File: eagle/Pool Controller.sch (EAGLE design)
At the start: 25 parts, among them J1 POWER_JACKPTH, J2 Temp_Pool, J4 Solar_Mon, J5 Temp_Solar, J6 Temp_Roof

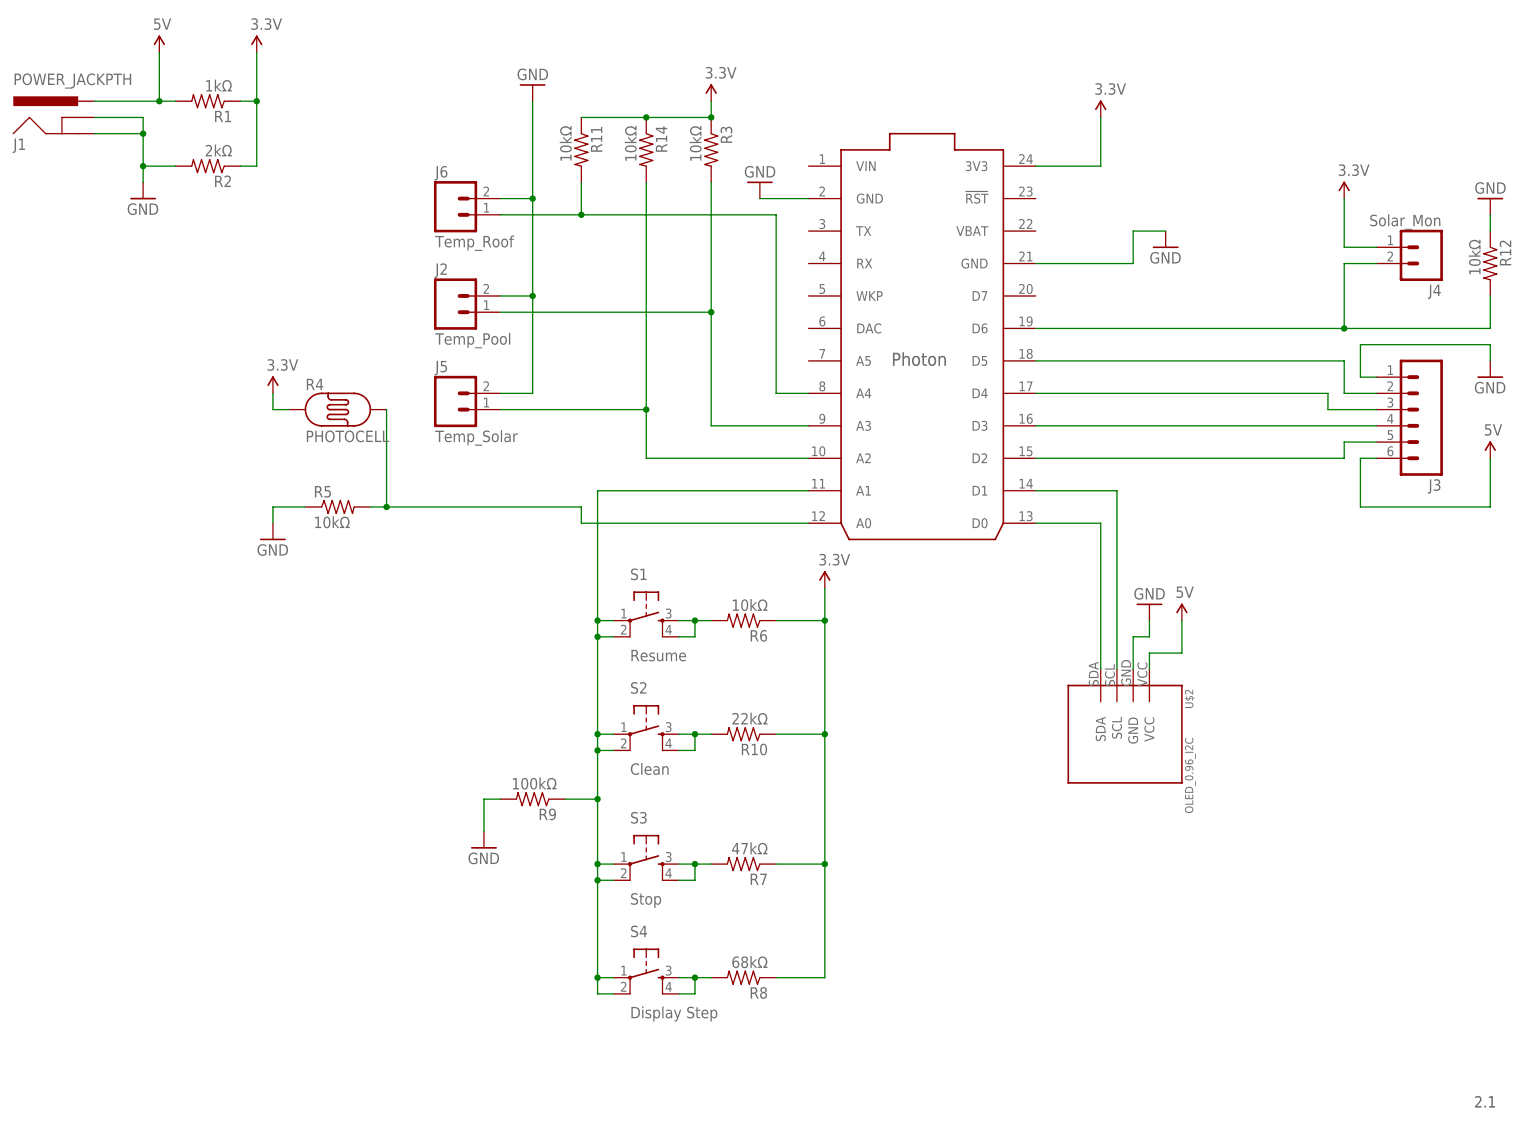
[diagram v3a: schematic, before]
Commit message: corrected relay pinout
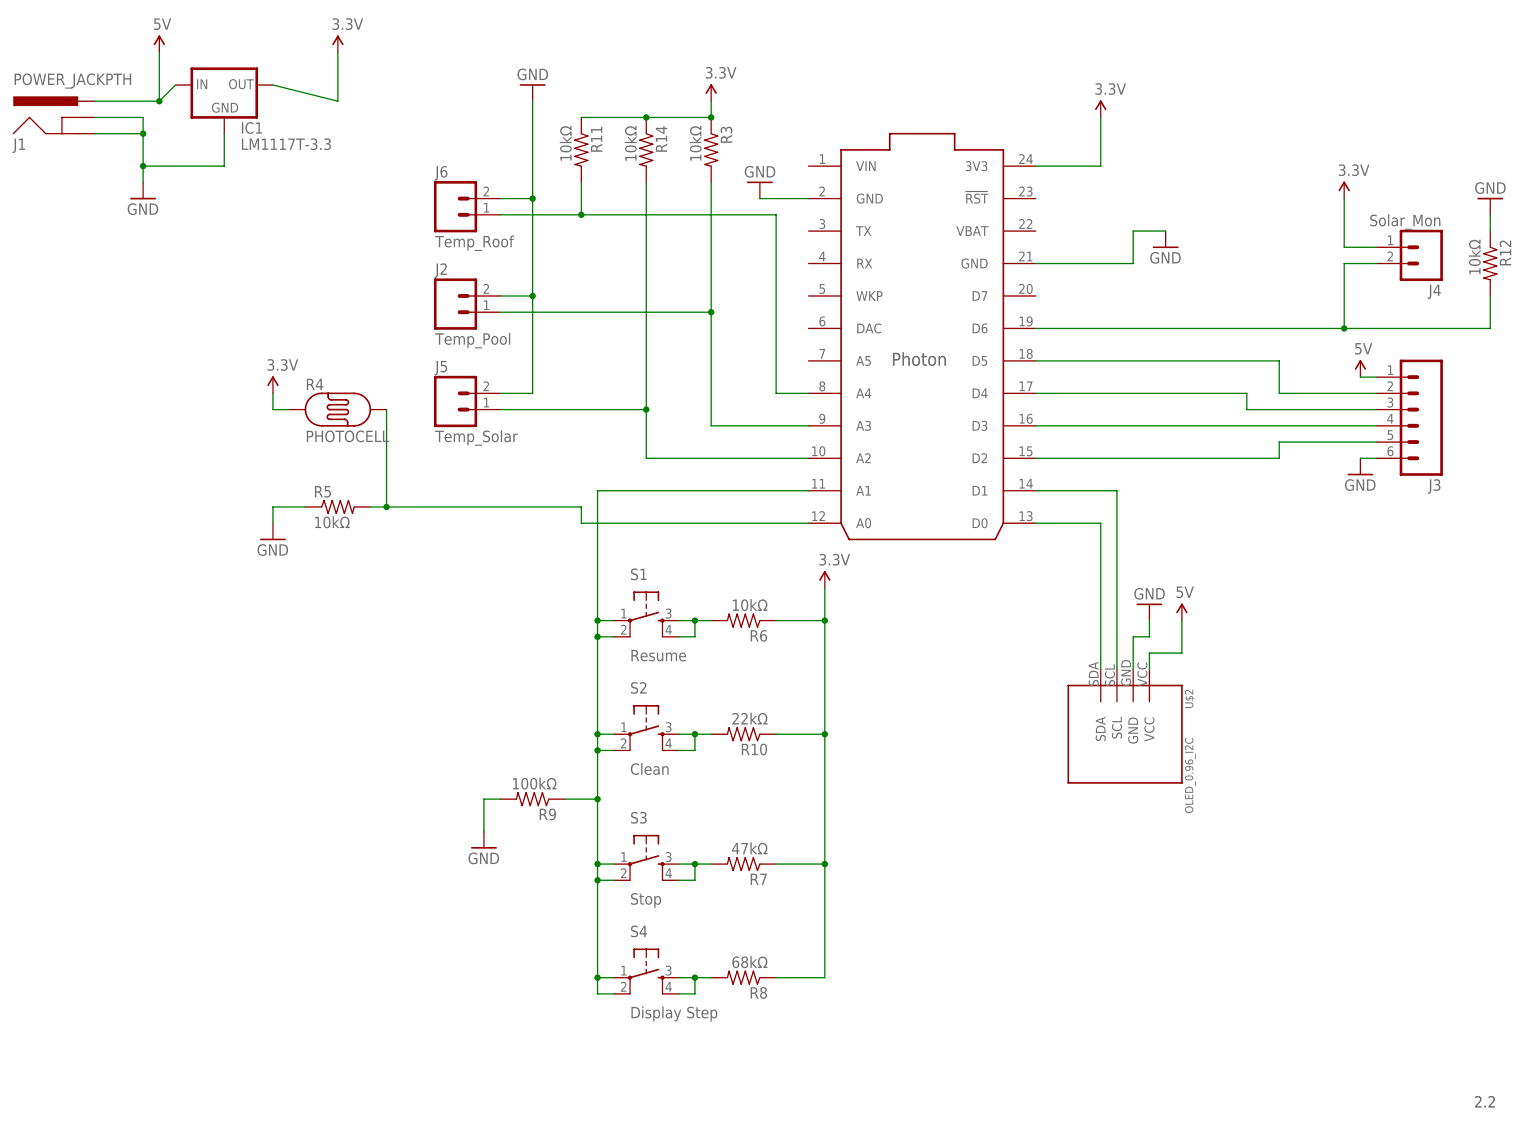
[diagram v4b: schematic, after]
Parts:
- removed R1: 1kΩ, SparkFun-Passives:RESISTORAXIAL-0.3
- removed R2: 2kΩ, SparkFun-Passives:RESISTORAXIAL-0.3
- added IC1: LM1117T-3.3, lm1117:LM1117T-3.3-V
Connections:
- net 3.3V: now also IC1.OUT; no longer R1.1, R2.1
- net 5V: now also IC1.IN, J3.1; no longer J3.6, R1.2
- net GND: now also IC1.GND, J3.6; no longer J3.1, R2.2
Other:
- note added: "2.2"
- note removed: "2.1"
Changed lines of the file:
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@@
 <part name="FRAME1" library="frames" deviceset="LETTER_L" device=""/>
 <part name="J1" library="SparkFun-Connectors" deviceset="POWER_JACK" device="PTH"/>
-<part name="R1" library="SparkFun-Passives" deviceset="RESISTOR" device="AXIAL-0.3" value="1kΩ"/>
-<part name="R2" library="SparkFun-Passives" deviceset="RESISTOR" device="AXIAL-0.3" value="2kΩ"/>
 <part name="R4" library="SparkFun-Sensors" deviceset="PHOTOCELL" device="PTH" value="PHOTOCELL"/>
 <part name="R5" library="SparkFun-Passives" deviceset="RESISTOR" device="AXIAL-0.3" value="10kΩ"/>
@@
 <part name="J6" library="SparkFun-Connectors" deviceset="M02" device="5MM" value="Temp_Roof"/>
 <part name="R11" library="SparkFun-Passives" deviceset="RESISTOR" device="AXIAL-0.3" value="10kΩ"/>
+<part name="IC1" library="lm1117" deviceset="LM1117T-*" device="-V" technology="3.3" value="LM1117T-3.3"/>
 </parts>
 <sheets>
 <sheet>
 <plain>
-<text x="233.68" y="-38.1" size="1.778" layer="97">2.1</text>
+<text x="233.68" y="-38.1" size="1.778" layer="97">2.2</text>
 </plain>
 <instances>
@@
 <instance part="FRAME1" gate="G$2" x="142.24" y="-45.72"/>
 <instance part="J1" gate="G$1" x="15.24" y="111.76"/>
-<instance part="R1" gate="G$1" x="35.56" y="119.38" rot="R180"/>
-<instance part="R2" gate="G$1" x="35.56" y="109.22" rot="R180"/>
 <instance part="R4" gate="G$1" x="55.88" y="71.12"/>
 <instance part="R5" gate="G$1" x="55.88" y="55.88"/>
 <instance part="GND1" gate="1" x="25.4" y="104.14"/>
-<instance part="SUPPLY1" gate="G$1" x="43.18" y="127"/>
+<instance part="SUPPLY1" gate="G$1" x="55.88" y="127"/>
 <instance part="SUPPLY2" gate="G$1" x="175.26" y="116.84"/>
 <instance part="GND2" gate="1" x="121.92" y="106.68" rot="R180"/>
@@
 <instance part="R10" gate="G$1" x="119.38" y="20.32" rot="R180"/>
 <instance part="J3" gate="G$1" x="223.52" y="71.12" rot="R180"/>
-<instance part="GND8" gate="1" x="236.22" y="76.2"/>
-<instance part="SUPPLY8" gate="G$1" x="236.22" y="63.5"/>
+<instance part="GND8" gate="1" x="215.9" y="60.96"/>
+<instance part="SUPPLY8" gate="G$1" x="215.9" y="76.2"/>
 <instance part="J4" gate="G$1" x="226.06" y="96.52" rot="R180"/>
 <instance part="J2" gate="G$1" x="73.66" y="86.36"/>
@@
 <instance part="J6" gate="G$1" x="73.66" y="101.6"/>
 <instance part="R11" gate="G$1" x="93.98" y="111.76" rot="R270"/>
+<instance part="IC1" gate="G$1" x="38.1" y="121.92"/>
 </instances>
 <busses>
@@
 <wire x1="17.78" y1="114.3" x2="25.4" y2="114.3" width="0.1524" layer="91"/>
 <junction x="25.4" y="114.3"/>
-<pinref part="R2" gate="G$1" pin="2"/>
-<wire x1="30.48" y1="109.22" x2="25.4" y2="109.22" width="0.1524" layer="91"/>
 <junction x="25.4" y="109.22"/>
+<pinref part="IC1" gate="G$1" pin="GND"/>
+<wire x1="38.1" y1="114.3" x2="38.1" y2="109.22" width="0.1524" layer="91"/>
+<wire x1="38.1" y1="109.22" x2="25.4" y2="109.22" width="0.1524" layer="91"/>
 </segment>
 <segment>
@@
 <pinref part="GND7" gate="1" pin="GND"/>
 <wire x1="78.74" y1="10.16" x2="78.74" y2="5.08" width="0.1524" layer="91"/>
-</segment>
-<segment>
-<pinref part="J3" gate="G$1" pin="1"/>
-<wire x1="218.44" y1="76.2" x2="215.9" y2="76.2" width="0.1524" layer="91"/>
-<wire x1="215.9" y1="76.2" x2="215.9" y2="81.28" width="0.1524" layer="91"/>
-<wire x1="215.9" y1="81.28" x2="236.22" y2="81.28" width="0.1524" layer="91"/>
-<pinref part="GND8" gate="1" pin="GND"/>
-<wire x1="236.22" y1="81.28" x2="236.22" y2="78.74" width="0.1524" layer="91"/>
 </segment>
 <segment>
@@
 <wire x1="45.72" y1="55.88" x2="45.72" y2="53.34" width="0.1524" layer="91"/>
 </segment>
+<segment>
+<pinref part="J3" gate="G$1" pin="6"/>
+<pinref part="GND8" gate="1" pin="GND"/>
+<wire x1="218.44" y1="63.5" x2="215.9" y2="63.5" width="0.1524" layer="91"/>
+</segment>
 </net>
 <net name="N$3" class="0">
@@
 <segment>
 <pinref part="J1" gate="G$1" pin="PWR"/>
-<pinref part="R1" gate="G$1" pin="2"/>
 <wire x1="17.78" y1="119.38" x2="27.94" y2="119.38" width="0.1524" layer="91"/>
 <pinref part="SUPPLY6" gate="G$1" pin="VCC"/>
-<wire x1="27.94" y1="119.38" x2="30.48" y2="119.38" width="0.1524" layer="91"/>
+<wire x1="27.94" y1="119.38" x2="30.48" y2="121.92" width="0.1524" layer="91"/>
 <wire x1="27.94" y1="127" x2="27.94" y2="119.38" width="0.1524" layer="91"/>
 <junction x="27.94" y="119.38"/>
+<pinref part="IC1" gate="G$1" pin="IN"/>
 </segment>
 <segment>
@@
 </segment>
 <segment>
-<pinref part="J3" gate="G$1" pin="6"/>
-<wire x1="218.44" y1="63.5" x2="215.9" y2="63.5" width="0.1524" layer="91"/>
-<wire x1="215.9" y1="63.5" x2="215.9" y2="55.88" width="0.1524" layer="91"/>
-<wire x1="215.9" y1="55.88" x2="236.22" y2="55.88" width="0.1524" layer="91"/>
+<pinref part="J3" gate="G$1" pin="1"/>
 <pinref part="SUPPLY8" gate="G$1" pin="VCC"/>
-<wire x1="236.22" y1="55.88" x2="236.22" y2="63.5" width="0.1524" layer="91"/>
-</segment>
-</net>
-<net name="N$1" class="0">
-<segment>
-<pinref part="PHOTON" gate="G$1" pin="D2"/>
-<wire x1="165.1" y1="63.5" x2="213.36" y2="63.5" width="0.1524" layer="91"/>
-<wire x1="213.36" y1="63.5" x2="213.36" y2="66.04" width="0.1524" layer="91"/>
-<pinref part="J3" gate="G$1" pin="5"/>
-<wire x1="213.36" y1="66.04" x2="218.44" y2="66.04" width="0.1524" layer="91"/>
-</segment>
-</net>
-<net name="N$2" class="0">
-<segment>
-<pinref part="PHOTON" gate="G$1" pin="D3"/>
-<wire x1="165.1" y1="68.58" x2="218.44" y2="68.58" width="0.1524" layer="91"/>
-<pinref part="J3" gate="G$1" pin="4"/>
-</segment>
-</net>
-<net name="N$7" class="0">
-<segment>
-<pinref part="PHOTON" gate="G$1" pin="D5"/>
-<wire x1="165.1" y1="78.74" x2="213.36" y2="78.74" width="0.1524" layer="91"/>
-<wire x1="213.36" y1="78.74" x2="213.36" y2="73.66" width="0.1524" layer="91"/>
-<pinref part="J3" gate="G$1" pin="2"/>
-<wire x1="213.36" y1="73.66" x2="218.44" y2="73.66" width="0.1524" layer="91"/>
+<wire x1="218.44" y1="76.2" x2="215.9" y2="76.2" width="0.1524" layer="91"/>
 </segment>
 </net>
@@
 </segment>
 </net>
-<net name="N$6" class="0">
-<segment>
-<wire x1="210.82" y1="73.66" x2="210.82" y2="71.12" width="0.1524" layer="91"/>
-<pinref part="J3" gate="G$1" pin="3"/>
-<wire x1="210.82" y1="71.12" x2="218.44" y2="71.12" width="0.1524" layer="91"/>
-<pinref part="PHOTON" gate="G$1" pin="D4"/>
-<wire x1="165.1" y1="73.66" x2="210.82" y2="73.66" width="0.1524" layer="91"/>
-</segment>
-</net>
 <net name="N$11" class="0">
 <segment>
@@
 </segment>
 <segment>
-<pinref part="R2" gate="G$1" pin="1"/>
-<wire x1="40.64" y1="109.22" x2="43.18" y2="109.22" width="0.1524" layer="91"/>
-<wire x1="43.18" y1="109.22" x2="43.18" y2="119.38" width="0.1524" layer="91"/>
 <pinref part="SUPPLY1" gate="G$1" pin="VCC"/>
-<pinref part="R1" gate="G$1" pin="1"/>
-<wire x1="43.18" y1="119.38" x2="43.18" y2="127" width="0.1524" layer="91"/>
-<wire x1="40.64" y1="119.38" x2="43.18" y2="119.38" width="0.1524" layer="91"/>
-<junction x="43.18" y="119.38"/>
+<wire x1="55.88" y1="119.38" x2="55.88" y2="127" width="0.1524" layer="91"/>
+<pinref part="IC1" gate="G$1" pin="OUT"/>
+<wire x1="55.88" y1="119.38" x2="45.72" y2="121.92" width="0.1524" layer="91"/>
 </segment>
 <segment>
@@
 </segment>
 </net>
+<net name="N$1" class="0">
+<segment>
+<pinref part="PHOTON" gate="G$1" pin="D2"/>
+<wire x1="165.1" y1="63.5" x2="203.2" y2="63.5" width="0.1524" layer="91"/>
+<wire x1="203.2" y1="63.5" x2="203.2" y2="66.04" width="0.1524" layer="91"/>
+<pinref part="J3" gate="G$1" pin="5"/>
+<wire x1="203.2" y1="66.04" x2="218.44" y2="66.04" width="0.1524" layer="91"/>
+</segment>
+</net>
+<net name="N$2" class="0">
+<segment>
+<pinref part="PHOTON" gate="G$1" pin="D3"/>
+<pinref part="J3" gate="G$1" pin="4"/>
+<wire x1="165.1" y1="68.58" x2="218.44" y2="68.58" width="0.1524" layer="91"/>
+</segment>
+</net>
+<net name="N$6" class="0">
+<segment>
+<pinref part="PHOTON" gate="G$1" pin="D4"/>
+<wire x1="165.1" y1="73.66" x2="198.12" y2="73.66" width="0.1524" layer="91"/>
+<wire x1="198.12" y1="73.66" x2="198.12" y2="71.12" width="0.1524" layer="91"/>
+<pinref part="J3" gate="G$1" pin="3"/>
+<wire x1="198.12" y1="71.12" x2="218.44" y2="71.12" width="0.1524" layer="91"/>
+</segment>
+</net>
+<net name="N$7" class="0">
+<segment>
+<pinref part="PHOTON" gate="G$1" pin="D5"/>
+<wire x1="165.1" y1="78.74" x2="203.2" y2="78.74" width="0.1524" layer="91"/>
+<wire x1="203.2" y1="78.74" x2="203.2" y2="73.66" width="0.1524" layer="91"/>
+<pinref part="J3" gate="G$1" pin="2"/>
+<wire x1="203.2" y1="73.66" x2="218.44" y2="73.66" width="0.1524" layer="91"/>
+</segment>
+</net>
